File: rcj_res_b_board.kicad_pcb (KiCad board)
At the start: 2 copper layers, 92.5 x 100 mm, 94 parts, among them P1 GP2Y0A41SK0F, P10 SERVO0, P11 MPU9250, P12 PING0, P13 CONN_01X03, P14 CONN_01X03, P15 CONN_01X04, P16 CONN_02X04, P2 GP2Y0A41SK0F, P3 GP2Y0A41SK0F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

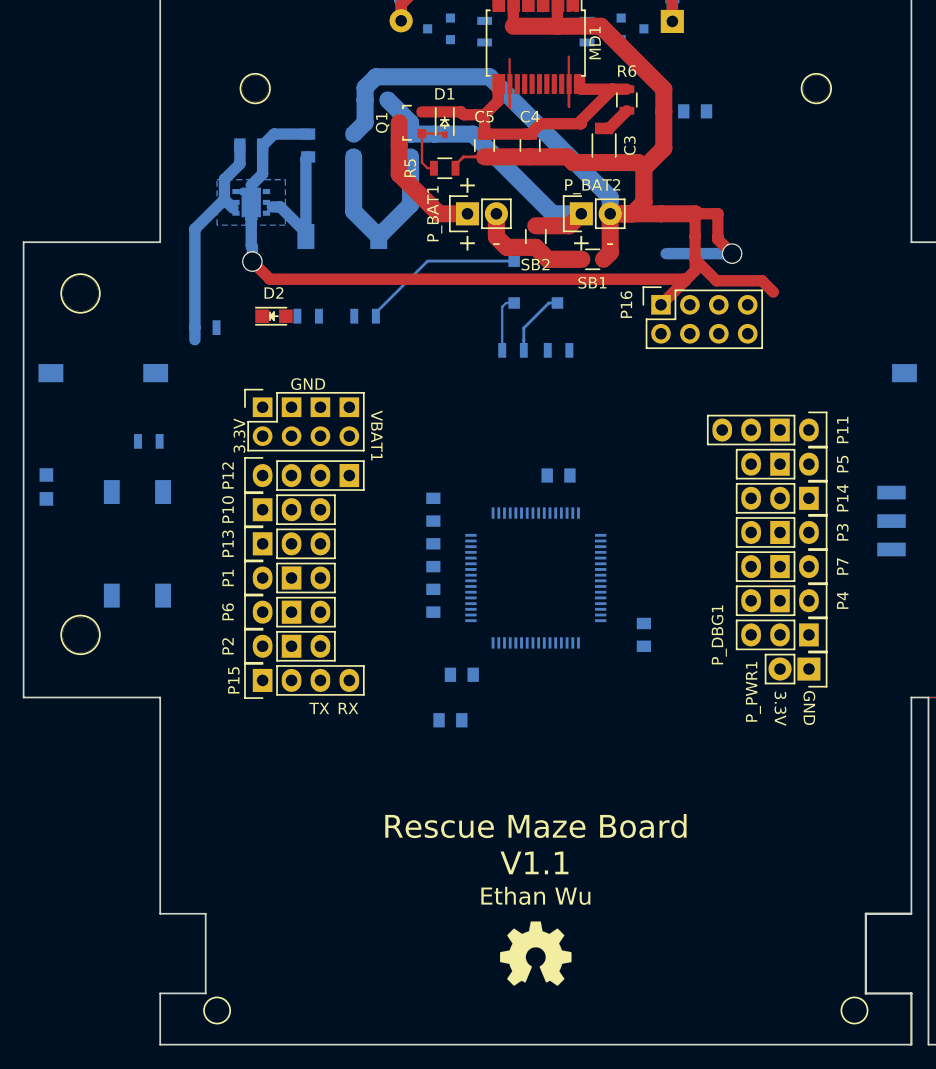
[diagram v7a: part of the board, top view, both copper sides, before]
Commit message: Changed drill hole size and moved decoupling cap
Shrunk drill hole for mounting dropper (2.3mm -> 2.1mm)
Moved motor driver decoupling cap closer to motor driver
Fixed incorrectly placed LED
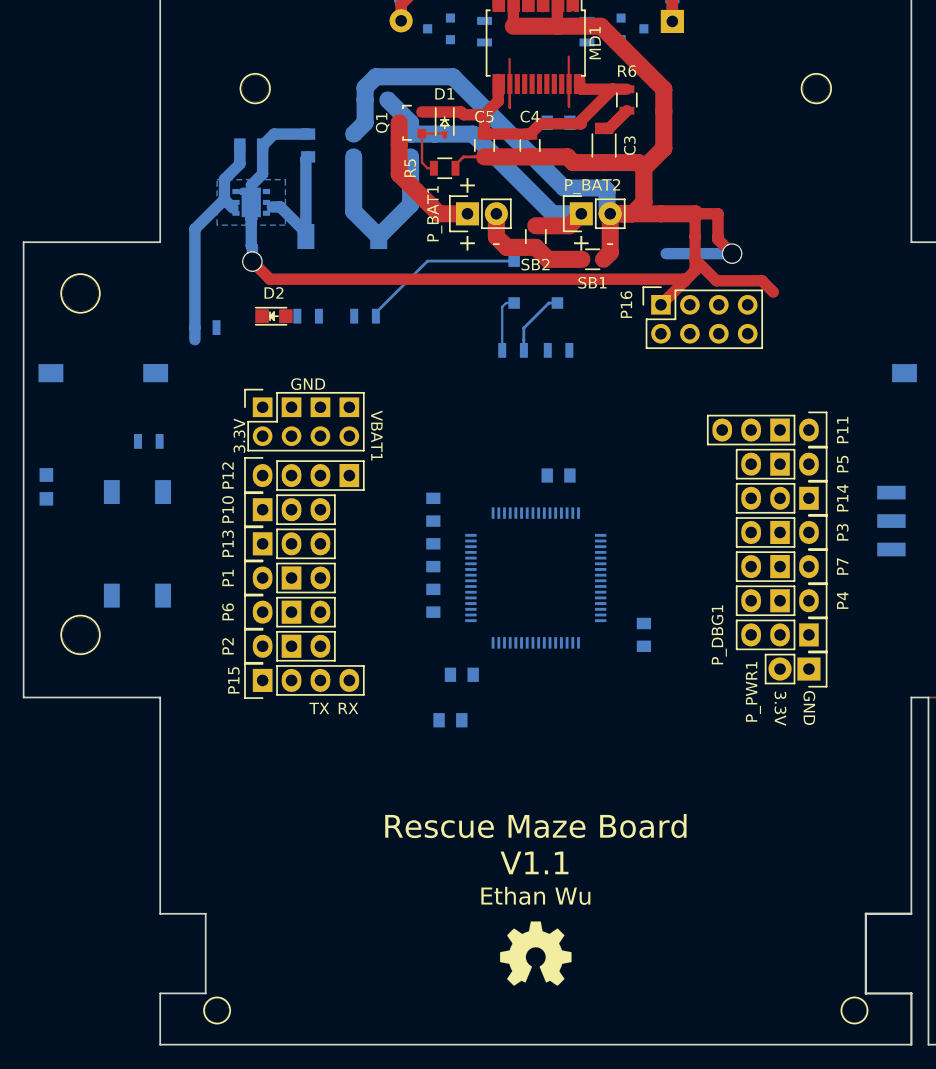
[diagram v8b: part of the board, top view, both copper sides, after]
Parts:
- moved C6 12.0 mm to (67.0, 69.0), turned to 0 degrees
- turned D4 to 90 degrees
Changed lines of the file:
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@@
 (kicad_pcb (version 4) (host pcbnew 0.201512291232+6408~40~ubuntu15.04.1-stable)
   (general
-    (links 228)
+    (links 0)
     (no_connects 168)
     (area 19.924999 49.924999 112.575001 150.100001)
     (thickness 1.6)
     (drawings 53)
-    (tracks 206)
+    (tracks 209)
     (zones 0)
     (modules 94)
@@
     (mod_text_size 1 1)
     (mod_text_width 0.15)
-    (pad_size 3.1 3.1)
-    (pad_drill 3.1)
+    (pad_size 2.1 2.1)
+    (pad_drill 2.1)
     (pad_to_mask_clearance 0.2)
     (aux_axis_origin 20 150)
@@
     )
     (fp_circle (center 0 0) (end 0 -1.15) (layer F.SilkS) (width 0.15))
-    (pad 1 thru_hole circle (at 0 0) (size 2.3 2.3) (drill 2.3) (layers *.Cu F.SilkS))
+    (pad 1 thru_hole circle (at 0 0) (size 2.1 2.1) (drill 2.1) (layers *.Cu F.SilkS))
   )
   (module Connect:1pin (layer F.Cu)
@@
     )
     (fp_circle (center 0 0) (end 0 -1.15) (layer F.SilkS) (width 0.15))
-    (pad 1 thru_hole circle (at 0 0) (size 2.3 2.3) (drill 2.3) (layers *.Cu F.SilkS))
+    (pad 1 thru_hole circle (at 0 0) (size 2.1 2.1) (drill 2.1) (layers *.Cu F.SilkS))
   )
   (module Custom:OPB733TR (layer B.Cu)
@@
   )
   (module Capacitors_SMD:C_0805 (layer B.Cu)
-    (at 79 68 180)
+    (at 67 69)
     (descr "Capacitor SMD 0805, reflow soldering, AVX (see smccp.pdf)")
     (tags "capacitor 0805")
     (attr smd)
-    (fp_text reference C6 (at 0 2.1 180) (layer B.SilkS)
+    (fp_text reference C6 (at 0 2.1) (layer B.SilkS)
       (effects (font (size 1 1) (thickness 0.15)) (justify mirror))
     )
-    (fp_text value 0.1uF (at 0 -2.1 180) (layer B.Fab)
+    (fp_text value 0.1uF (at 0 -2.1) (layer B.Fab)
       (effects (font (size 1 1) (thickness 0.15)) (justify mirror))
     )
@@
     (fp_line (start 0.5 0.85) (end -0.5 0.85) (layer B.SilkS) (width 0.15))
     (fp_line (start -0.5 -0.85) (end 0.5 -0.85) (layer B.SilkS) (width 0.15))
-    (pad 1 smd rect (at -1 0 180) (size 1 1.25) (layers B.Cu B.Paste B.Mask)
+    (pad 1 smd rect (at -1 0) (size 1 1.25) (layers B.Cu B.Paste B.Mask)
       (net 2 GNDD))
-    (pad 2 smd rect (at 1 0 180) (size 1 1.25) (layers B.Cu B.Paste B.Mask)
+    (pad 2 smd rect (at 1 0) (size 1 1.25) (layers B.Cu B.Paste B.Mask)
       (net 3 /3.3V))
     (model Capacitors_SMD.3dshapes/C_0805.wrl
@@
   )
   (module LEDs:LED-0805 (layer B.Cu)
-    (at 22 101 270)
+    (at 22 101 90)
     (descr "LED 0805 smd package")
     (tags "LED 0805 SMD")
     (attr smd)
-    (fp_text reference D4 (at 0 1.75 270) (layer B.SilkS)
+    (fp_text reference D4 (at 0 1.75 90) (layer B.SilkS)
       (effects (font (size 1 1) (thickness 0.15)) (justify mirror))
     )
-    (fp_text value LED (at 0 -1.75 270) (layer B.Fab)
+    (fp_text value LED (at 0 -1.75 90) (layer B.Fab)
       (effects (font (size 1 1) (thickness 0.15)) (justify mirror))
     )
@@
     (fp_line (start -1.9 -0.95) (end -1.9 0.95) (layer B.CrtYd) (width 0.05))
     (fp_line (start -1.9 0.95) (end 1.9 0.95) (layer B.CrtYd) (width 0.05))
-    (pad 2 smd rect (at 1.04902 0 90) (size 1.19888 1.19888) (layers B.Cu B.Paste B.Mask)
+    (pad 2 smd rect (at 1.04902 0 270) (size 1.19888 1.19888) (layers B.Cu B.Paste B.Mask)
       (net 76 "Net-(D4-Pad2)"))
-    (pad 1 smd rect (at -1.04902 0 90) (size 1.19888 1.19888) (layers B.Cu B.Paste B.Mask)
+    (pad 1 smd rect (at -1.04902 0 270) (size 1.19888 1.19888) (layers B.Cu B.Paste B.Mask)
       (net 2 GNDD))
     (model LEDs.3dshapes/LED-0805.wrl
@@
   )
   (gr_circle (center 40.35 48) (end 40.35 49.15) (layer Cmts.User) (width 0.2))
-  (gr_text GND (at 45 92 360) (layer F.SilkS)
+  (gr_text GND (at 45 92) (layer F.SilkS)
     (effects (font (size 1 1) (thickness 0.2)))
   )
@@
   (segment (start 54 72) (end 54 76.2) (width 1.5) (layer B.Cu) (net 6))
   (segment (start 54 76.2) (end 51.2 79) (width 1.5) (layer B.Cu) (net 6))
+  (segment (start 71.54 77) (end 71.266001 77) (width 1.5) (layer B.Cu) (net 32))
+  (segment (start 71.266001 77) (end 71.266001 74.983999) (width 1.5) (layer B.Cu) (net 32))
+  (segment (start 50 65.918277) (end 50 67) (width 1.5) (layer B.Cu) (net 32))
+  (segment (start 71.266001 74.983999) (end 71.016001 74.733999) (width 1.5) (layer B.Cu) (net 32))
+  (segment (start 71.016001 74.733999) (end 67.489685 74.733999) (width 1.5) (layer B.Cu) (net 32))
+  (segment (start 57.722523 64.966837) (end 50.95144 64.966837) (width 1.5) (layer B.Cu) (net 32))
+  (segment (start 67.489685 74.733999) (end 57.722523 64.966837) (width 1.5) (layer B.Cu) (net 32))
+  (segment (start 50.95144 64.966837) (end 50 65.918277) (width 1.5) (layer B.Cu) (net 32))
   (segment (start 71.54 77) (end 76 77) (width 1.5) (layer F.Cu) (net 32))
   (segment (start 71.54 77) (end 73.5 77) (width 1.5) (layer F.Cu) (net 32))
@@
   (segment (start 71.54 77) (end 71.54 80.41) (width 1.5) (layer F.Cu) (net 32))
   (segment (start 71.54 80.41) (end 70.95 81) (width 1.5) (layer F.Cu) (net 32))
-  (segment (start 71.54 77) (end 71.54 75.56316) (width 1.5) (layer B.Cu) (net 32))
-  (segment (start 71.54 75.56316) (end 60.943677 64.966837) (width 1.5) (layer B.Cu) (net 32))
-  (segment (start 60.943677 64.966837) (end 50.95144 64.966837) (width 1.5) (layer B.Cu) (net 32))
-  (segment (start 50.95144 64.966837) (end 50 65.918277) (width 1.5) (layer B.Cu) (net 32))
-  (segment (start 50 65.918277) (end 50 67) (width 1.5) (layer B.Cu) (net 32))
   (segment (start 50 67) (end 50 69) (width 1.5) (layer B.Cu) (net 32))
   (segment (start 50 69) (end 49 70) (width 1.5) (layer B.Cu) (net 32))
